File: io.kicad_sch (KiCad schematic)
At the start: 26 parts, among them CN3 DF40C-30DS-0.4V | IO, J1 USB3_A, J6 Micro_SD_Card_Det1, U12 GL850G-HHY22, U7 USBLC6-2P6, Y1 Crystal

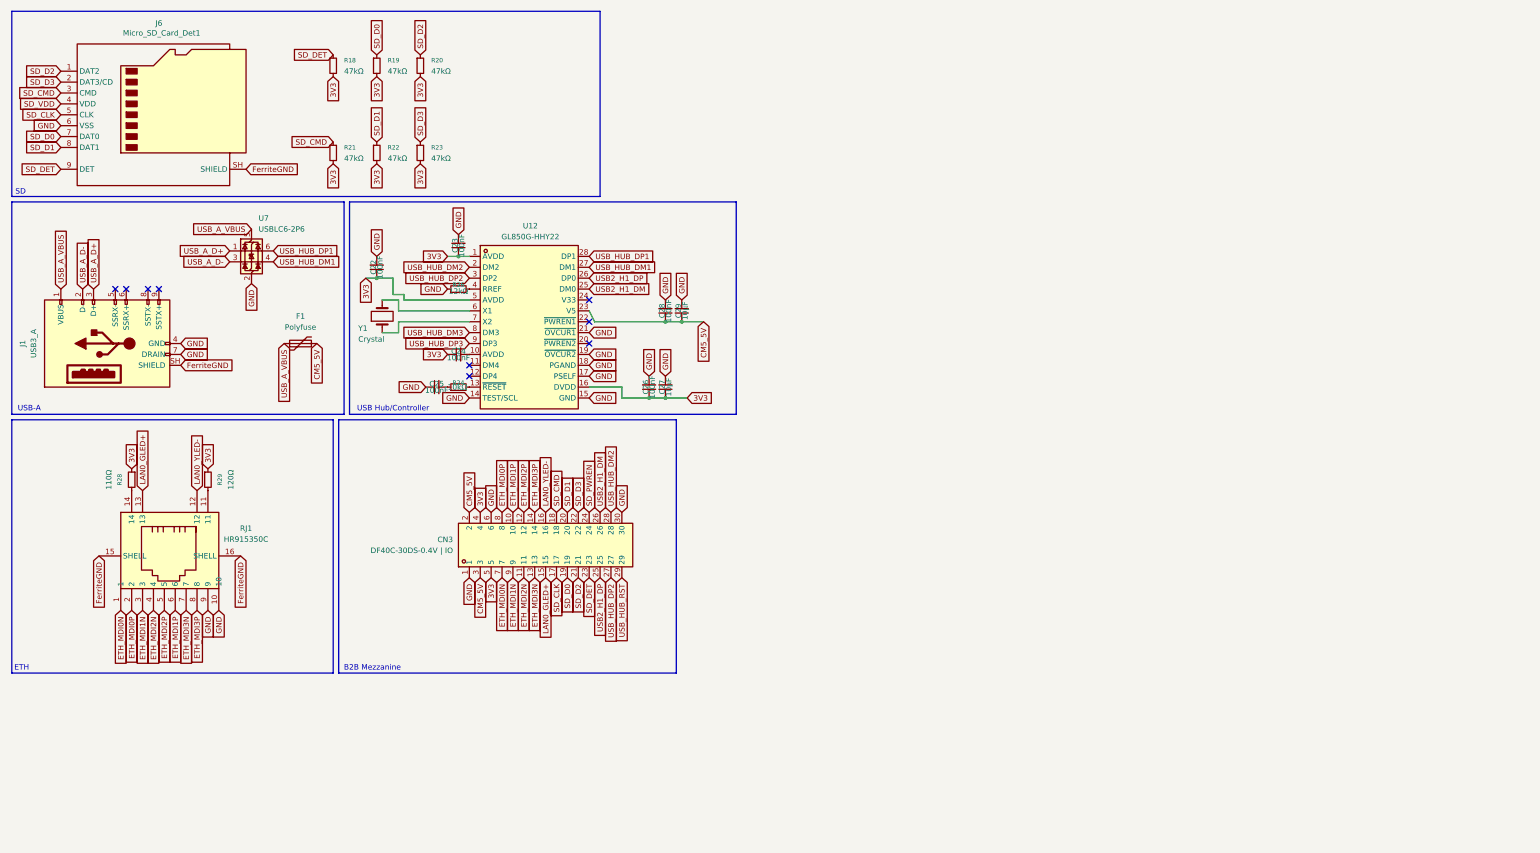
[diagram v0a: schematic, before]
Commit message: Move Data USB-C Port to IO + Add USB1 SS mux and SBU orientation switch, resolve CM5 GPIO assignments
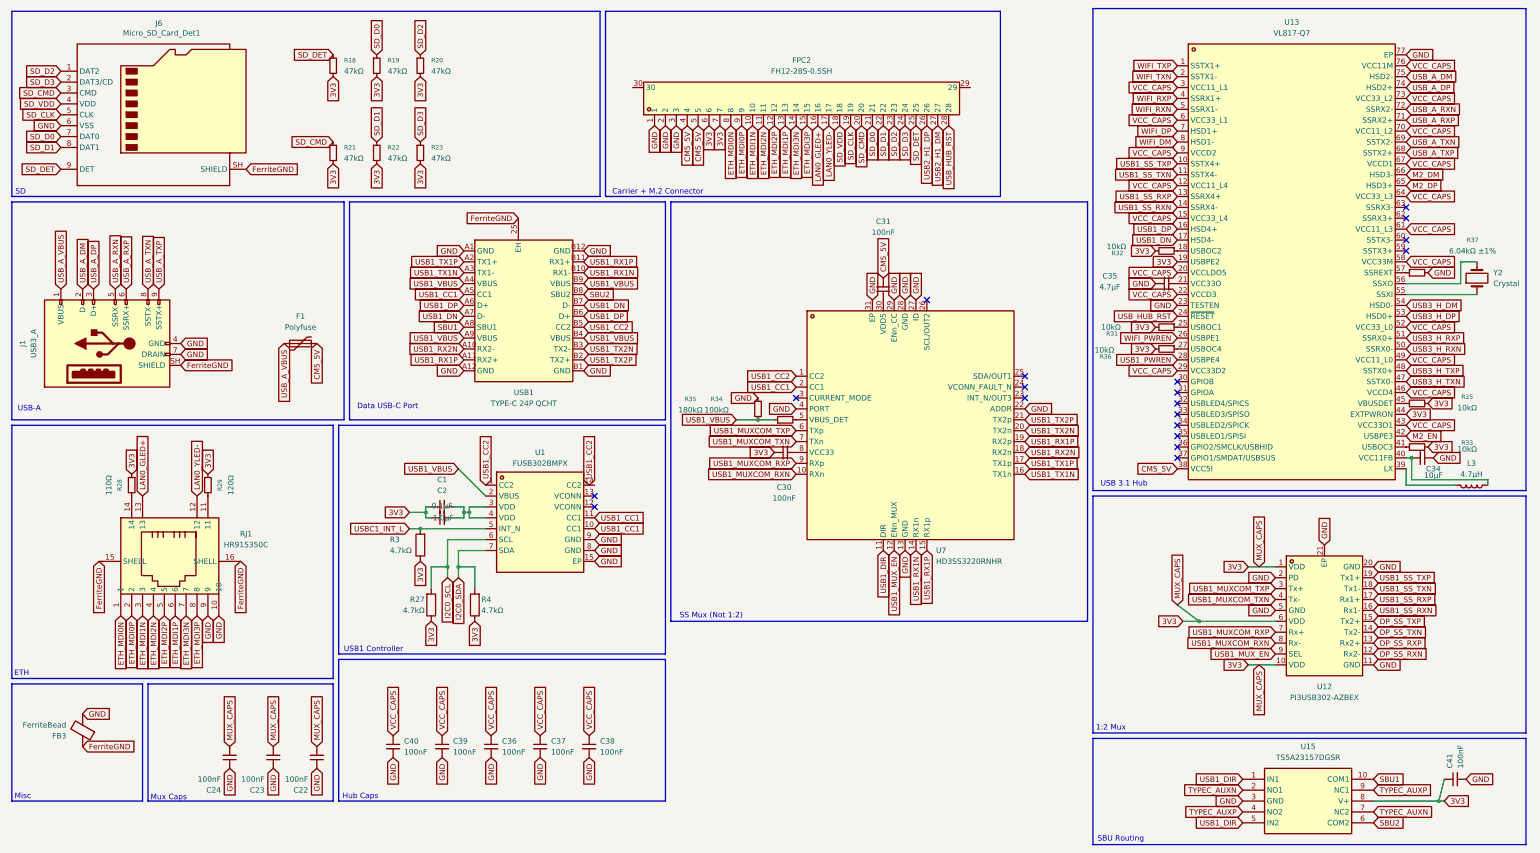
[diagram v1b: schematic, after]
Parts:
- removed C25, C26, C28: 100nF, symbol Device:C_Small
- removed C27, C29: 10µF, symbol Device:C_Small
- removed CN3: DF40C-30DS-0.4V | IO, slate113:CONN-SMD_DF40C-30DS-0.4V51, symbol slate113:DF40C-30DS-0.4V
- removed R24: 10kΩ, symbol Device:R_Small
- removed R26: 12kΩ, symbol Device:R_Small
- removed U12: GL850G-HHY22, slate113:SSOP-28_L10.2-W5.3-P0.65-LS7.8-BL, symbol slate113:GL850G-HHY22
- removed U7: USBLC6-2P6, Package_TO_SOT_SMD:SOT-666, symbol Power_Protection:USBLC6-2P6
- removed Y1: Crystal, symbol Device:Crystal
- added C1: 0.1µF, symbol Device:C_Small
- added C2: 1.0µF, symbol Device:C_Small
- added C30, C31, C36, C37, C38, C39, C40, C41: 100nF, symbol Device:C_Small
- added C34: 10µF, symbol Device:C_Small
- added C35: 4.7µF, symbol Device:C_Small
- added FB3: FerriteBead, symbol Device:FerriteBead
- added FPC2: FH12-28S-0.5SH, slate113:FPC-SMD_28P-P0.50_FH12-28S-0.5SH-55, symbol slate113:FH12-28S-0.5SH
- added L3: 4.7µH, symbol Device:L
- added R25, R31, R32, R33, R36: 10kΩ, symbol Device:R_Small
- added R27, R3, R4: 4.7kΩ, symbol Device:R
- added R34: 100kΩ, symbol Device:R_Small
- added R35: 180kΩ, symbol Device:R_Small
- added R37: 6.04kΩ ±1%, symbol Device:R_Small
- added U1: FUSB302BMPX, slate113:MLP-14_L2.5-W2.5-P0.50-BL-EP, symbol slate113:FUSB302BMPX
- added U12: PI3USB302-AZBEX, slate113:DHVQFN-20_L4.5-W2.5-P0.50-BL-EP, symbol slate113:PI3USB302-AZBEX
- added U13: VL817-Q7, slate113:QFN-76_L9.0-W9.0-P0.40-BL-EP, symbol slate113:VL817-Q7
- added U15: TS5A23157DGSR, slate113:MSOP-10_L3.0-W3.0-P0.50-LS5.0-BL, symbol slate113:TS5A23157DGSR
- added U7: HD3SS3220RNHR, slate113:WQFN-30_L4.5-W2.5-P0.4-BL-EP, symbol slate113:HD3SS3220RNHR
- added USB1: TYPE-C 24P QCHT, slate113:TYPE-C-SMD_TYPE-C-24P-QCHT, symbol slate113:TYPE-C24PQCHT
- added Y2: Crystal, symbol Device:Crystal
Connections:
- net 3V3: now also C22.2, C23.2, C24.2, C1.1, C2.1, C30.1, C41.1, FPC2.6, FPC2.7, R25.2, R27.1, R3.1, R31.2, R32.2, R33.2, R36.2, R4.1, U12.1 (VDD), U12.10 (VDD), U12.6 (VDD), U13.19 (USBPE2), U13.44 (EXTPWRON), U15.8 (V+); no longer C22.1, C23.1, C24.1
- net CM5_5V: now also C31.2, FPC2.4, FPC2.5, U13.38 (VCC5I)
- net ETH_MDI0N: now also FPC2.8
- net ETH_MDI0P: now also FPC2.9
- net ETH_MDI1N: now also FPC2.10
- net ETH_MDI1P: now also FPC2.13
- net ETH_MDI2N: now also FPC2.11
- net ETH_MDI2P: now also FPC2.12
- net ETH_MDI3N: now also FPC2.14
- net ETH_MDI3P: now also FPC2.15
- net FerriteGND: now also FB3.1, USB1.25 (EH)
- net GND: now also C22.1, C23.1, C24.1, C34.1, C35.1, C36.2, C37.2, C38.2, C39.2, C40.2, C41.2, FB3.2, FPC2.1, FPC2.2, FPC2.3, R35.1, R37.2, U1.15 (EP), U1.8 (GND), U1.9 (GND), U12.11 (GND), U12.2 (PD), U12.20 (GND), U12.21 (EP), U12.5 (GND), U13.23 (TESTEN), U13.77 (EP), U15.3 (GND), U7.13 (GND), U7.22 (ADDR), U7.27 (ID), U7.28 (GND), U7.29 (ENn_CC), U7.31 (EP), U7.4 (PORT), USB1.A1 (GND), USB1.A12 (GND), USB1.B1 (GND), USB1.B12 (GND); no longer C22.2, C23.2
- net LAN0_GLED+: now also FPC2.16
- net LAN0_YLED-: now also FPC2.17
- net SD_CLK: now also FPC2.19
- net SD_CMD: now also FPC2.20
- net SD_D0: now also FPC2.21
- net SD_D1: now also FPC2.22
- net SD_D2: now also FPC2.23
- net SD_D3: now also FPC2.24
- net SD_DET: now also FPC2.25
- net SD_VDD: now also FPC2.18
- net USB2_H1_DM: now also FPC2.27
- net USB2_H1_DP: now also FPC2.26
- net USB_HUB_RST: now also FPC2.28, U13.24 (~{RESET})
- net USB_A_RXN: now reaches J1.5 (SSRX-)
- net USB_A_RXN: now also U13.72 (SSRX2-)
- net USB_A_RXP: now reaches J1.6 (SSRX+)
- net USB_A_RXP: now also U13.71 (SSRX2+)
- net USB_A_TXN: now reaches J1.8 (SSTX-)
- net USB_A_TXN: now also U13.69 (SSTX2-)
- net USB_A_TXP: now reaches J1.9 (SSTX+)
- net USB_A_TXP: now also U13.68 (SSTX2+)
- net USB_A_D+ renamed USB_A_DP
- net USB_A_DP: now also U13.74 (HSD2+)
- net USB_A_D- renamed USB_A_DM
- net USB_A_DM: now also U13.75 (HSD2-)
- new net: C31.1, U7.30 (VDD5)
- new net: R31.1, U13.25 (USBOC1)
- new net: C1.2, C2.2, U1.3 (VDD), U1.4 (VDD)
- new net: R32.1, U13.18 (USBOC2)
- new net: C35.2, U13.21 (VCC33O)
- new net: R36.1, U13.27 (USBOC4)
- new net: L3.2, U13.39 (LX)
- new net: C34.2, L3.1, U13.40 (VCC11FB)
- new net: R33.1, U13.41 (USBOC3)
- new net: R25.1, U13.45 (VBUSDET)
- new net: U13.55 (SSXI), Y2.1
- new net: U13.56 (SSXO), Y2.2
- new net: R37.1, U13.57 (SSREXT)
- new net: R34.2, U7.5 (VBUS_DET)
- new net: C30.2, U7.8 (VCC33)
- new net DP_SS_RXN: U12.12 (Rx2-)
- new net DP_SS_RXP: U12.13 (Rx2+)
- new net DP_SS_TXN: U12.14 (Tx2-)
- new net DP_SS_TXP: U12.15 (Tx2+)
- new net I2C0_SCL: R27.2, U1.6 (SCL)
- new net I2C0_SDA: R4.2, U1.7 (SDA)
- new net M2_DM: U13.66 (HSD3-)
- new net M2_DP: U13.65 (HSD3+)
- new net M2_EN: U13.42 (USBPE3)
- new net SBU1: U15.10 (COM1), USB1.A8 (SBU1)
- new net SBU2: U15.6 (COM2), USB1.B8 (SBU2)
- new net TYPEC_AUXN: U15.2 (NO1), U15.7 (NC2)
- new net TYPEC_AUXP: U15.4 (NO2), U15.9 (NC1)
- new net USB1_CC1: U1.10 (CC1), U1.11 (CC1), U7.2 (CC1), USB1.A5 (CC1)
- new net USB1_CC2: U1.1 (CC2), U7.1 (CC2), USB1.B5 (CC2)
- new net USB1_DIR: U15.1 (IN1), U15.5 (IN2), U7.11 (DIR)
- new net USB1_DN: U13.17 (HSD4-), USB1.A7 (D-), USB1.B7 (D-)
- new net USB1_DP: U13.16 (HSD4+), USB1.A6 (D+), USB1.B6 (D+)
- new net USB1_MUXCOM_RXN: U12.8 (Rx-), U7.10 (RXn)
- new net USB1_MUXCOM_RXP: U12.7 (Rx+), U7.9 (RXp)
- new net USB1_MUXCOM_TXN: U12.4 (Tx-), U7.7 (TXn)
- new net USB1_MUXCOM_TXP: U12.3 (Tx+), U7.6 (TXp)
- new net USB1_MUX_EN: U12.9 (SEL), U7.12 (ENn_MUX)
- new net USB1_PWREN: U13.28 (USBPE4)
- new net USB1_RX1N: U7.14 (RX1n), USB1.B10 (RX1-)
- new net USB1_RX1P: U7.15 (RX1p), U7.19 (RX2p), USB1.A11 (RX2+), USB1.B11 (RX1+)
- new net USB1_RX2N: U7.18 (RX2n), USB1.A10 (RX2-)
- new net USB1_SS_RXN: U12.16 (Rx1-), U13.14 (SSRX4-)
- new net USB1_SS_RXP: U12.17 (Rx1+), U13.13 (SSRX4+)
- new net USB1_SS_TXN: U12.18 (Tx1-), U13.11 (SSTX4-)
- new net USB1_SS_TXP: U12.19 (Tx1+), U13.10 (SSTX4+)
- new net USB1_TX1N: U7.16 (TX1n), USB1.A3 (TX1-)
- new net USB1_TX1P: U7.17 (TX1p), USB1.A2 (TX1+)
- new net USB1_TX2N: U7.20 (TX2n), USB1.B3 (TX2-)
- new net USB1_TX2P: U7.21 (TX2p), USB1.B2 (TX2+)
- new net USB1_VBUS: R34.1, R35.2, U1.2 (VBUS), USB1.A4 (VBUS), USB1.A9 (VBUS), USB1.B4 (VBUS), USB1.B9 (VBUS)
- new net USB3_H_DM: U13.54 (HSD0-)
- new net USB3_H_DP: U13.53 (HSD0+)
- new net USB3_H_RXN: U13.50 (SSRX0-)
- new net USB3_H_RXP: U13.51 (SSRX0+)
- new net USB3_H_TXN: U13.47 (SSTX0-)
- new net USB3_H_TXP: U13.48 (SSTX0+)
- new net USBC1_INT_L: R3.2, U1.5 (INT_N)
- new net VCC_CAPS: C36.1, C37.1, C38.1, C39.1, C40.1, U13.12 (VCC11_L4), U13.15 (VCC33_L4), U13.20 (VCCLDO5), U13.22 (VCCD3), U13.29 (VCC33D2), U13.3 (VCC11_L1), U13.43 (VCC33D1), U13.46 (VCCD4), U13.49 (VCC11_L0), U13.52 (VCC33_L0), U13.58 (VCC33M), U13.6 (VCC33_L1), U13.61 (VCC11_L3), U13.64 (VCC33_L3), U13.67 (VCCD1), U13.70 (VCC11_L2), U13.73 (VCC33_L2), U13.76 (VCC11M), U13.9 (VCCD2)
- new net WIFI_DM: U13.8 (HSD1-)
- new net WIFI_DP: U13.7 (HSD1+)
- new net WIFI_PWREN: U13.26 (USBPE1)
- new net WIFI_RXN: U13.5 (SSRX1-)
- new net WIFI_RXP: U13.4 (SSRX1+)
- new net WIFI_TXN: U13.2 (SSTX1-)
- new net WIFI_TXP: U13.1 (SSTX1+)
- no-connect marks 9 -> 19
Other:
- note added: "1:2 Mux"
- note added: "Carrier + M.2 Connector"
- note added: "Data USB-C Port"
- note added: "Hub Caps"
- note added: "Misc"
- note added: "Mux Caps"
- note added: "SBU Routing"
- note added: "SS Mux (Not 1:2)"
- note added: "USB 3.1 Hub"
- note added: "USB1 Controller"
- note removed: "B2B Mezzanine"
- note removed: "USB Hub/Controller"
- moved on the sheet: R28, R29, RJ1

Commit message: add wifi+ble combo symbol, fix connector pin counts, slim b2b connectors, drop 3-way flex cable
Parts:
- removed C35: 4.7µF, symbol Device:C_Small
- removed FPC2: FH12-28S-0.5SH, slate113:FPC-SMD_28P-P0.50_FH12-28S-0.5SH-55, symbol slate113:FH12-28S-0.5SH
- added C18, C32, C42: 2.2µF, symbol Device:C_Small
- added C20, C26, C27, C33, C43, C44, C45, C46, C47, C48, C49, C50, C51, C52, C53, C54, C55, C56: 100nF, symbol Device:C_Small
- added CN2: DF40C-40DP-0.4V, slate113:CONN-SMD_DF40C-40DP-0.4V, symbol slate113:DF40C-40DP-0.4V
- added R24: 10kΩ, symbol Device:R_Small
- added U10, U14, U17: SiP32508DT, Package_TO_SOT_SMD:TSOT-23-6, symbol Power_Management:SiP32508DT
- added U16: (no value), symbol slate113:AMLGA7921
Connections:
- net 3V3: now also C18.1, C42.1, CN2.6, CN2.7, R24.1
- net CM5_5V: now also C32.1, CN2.4, CN2.5
- net DP_SS_RXN: now also CN2.34
- net DP_SS_RXP: now also CN2.33
- net DP_SS_TXN: now also CN2.32
- net DP_SS_TXP: now also CN2.31
- net ETH_MDI0N: now also CN2.8
- net ETH_MDI0P: now also CN2.9
- net ETH_MDI1N: now also CN2.10
- net ETH_MDI1P: now also CN2.13
- net ETH_MDI2N: now also CN2.11
- net ETH_MDI2P: now also CN2.12
- net ETH_MDI3N: now also CN2.14
- net ETH_MDI3P: now also CN2.15
- net FerriteGND: now also CN2.39, CN2.41, CN2.42, CN2.43, CN2.44
- net GND: now also C26.1, C27.1, C44.2, C45.2, C46.2, C47.2, C48.2, C49.2, C50.2, C51.2, C52.2, C53.2, C54.2, C55.2, C56.2, CN2.1, CN2.2, CN2.3, U10.4 (GND), U14.4 (GND), U16.14 (GND), U16.15 (GND), U16.18 (GND), U16.19 (GND), U16.21 (GND), U16.22 (GND), U16.29 (GND), U16.3 (GND), U16.6 (GND), U16.9 (GND), U17.4 (GND)
- net I2C0_SCL: now also CN2.37
- net I2C0_SDA: now also CN2.38
- net LAN0_GLED+: now also CN2.16
- net LAN0_YLED-: now also CN2.17
- net M2_DM: now also CN2.27
- net M2_DP: now also CN2.26
- net M2_EN: now also CN2.40
- net SD_CLK: now also CN2.19
- net SD_CMD: now also CN2.20
- net SD_D0: now also CN2.21
- net SD_D1: now also CN2.22
- net SD_D2: now also CN2.23
- net SD_D3: now also CN2.24
- net SD_DET: now also CN2.25
- net SD_VDD: now also C20.1
- net TYPEC_AUXN: now also CN2.36
- net TYPEC_AUXP: now also CN2.35
- net USB1_DIR: now also CN2.30
- net USB1_MUX_EN: now also CN2.29
- net USB1_PWREN: now also U14.3 (EN)
- net USB1_VBUS: now also C33.1
- net USB_HUB_RST: now also CN2.28
- net VCC_CAPS: now also U13.21 (VCC33O), C44.1, C45.1, C46.1, C47.1, C48.1, C49.1, C50.1, C51.1, C52.1, C53.1, C54.1, C55.1, C56.1
- net WIFI_DM: now also U16.8 (USB_DM)
- net WIFI_DP: now also U16.7 (USB_DP)
- net WIFI_PWREN: now also U17.3 (EN)
- net WIFI_RXN: now also U16.4 (SSUSB_RXN)
- net WIFI_RXP: now also U16.5 (SSUSB_RXP)
- net WIFI_TXN: now also U16.1 (SSUSB_TXN)
- net WIFI_TXP: now also U16.2 (SSUSB_TXP)
- new net: C32.2, U14.5 (IN), U14.6 (IN)
- new net: C43.2, U17.1 (OUT), U17.2 (OUT)
- new net: C20.2, U10.1 (OUT), U10.2 (OUT)
- new net: C18.2, U10.5 (IN), U10.6 (IN)
- new net: R24.2, U16.26 (#RST)
- new net: C42.2, U17.5 (IN), U17.6 (IN)
- new net: C33.2, U14.1 (OUT), U14.2 (OUT)
- new net BT_WAKE: U16.11 (#BT_WAKE)
- new net SD_PWREN: CN2.18, U10.3 (EN)
- new net WIFI_CAPS: C26.2, C27.2, C43.1, U16.27 (DVDD), U16.28 (DVDD)
- new net WOWLAN: U16.10 (#WOWLAN)
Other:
- note added: "Controller"
- note added: "SD Power"
- note added: "USB1 Power"
- note added: "WiFi Module"
- note added: "WiFi Power"
- moved on the sheet: C36, C37, C38, C39, C40

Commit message: finish wiring up usb hub + fix stale nets + address DRC errors
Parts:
- removed CN2: DF40C-40DP-0.4V, slate113:CONN-SMD_DF40C-40DP-0.4V, symbol slate113:DF40C-40DP-0.4V
- added CN1: DF40C-50DP-0.4V, slate113:CONN-SMD_DF40C-50DP-0.4V, symbol slate113:DF40C-50DP-0.4V
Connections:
- net 3V3: now also CN1.6, CN1.7
- net CM5_5V: now also CN1.4, CN1.5
- net DP_SS_RXN: now also CN1.34
- net DP_SS_RXP: now also CN1.33
- net DP_SS_TXN: now also CN1.32
- net DP_SS_TXP: now also CN1.31
- net ETH_MDI0N: now also CN1.8
- net ETH_MDI0P: now also CN1.9
- net ETH_MDI1N: now also CN1.10
- net ETH_MDI1P: now also CN1.13
- net ETH_MDI2N: now also CN1.11
- net ETH_MDI2P: now also CN1.12
- net ETH_MDI3N: now also CN1.14
- net ETH_MDI3P: now also CN1.15
- net FerriteGND: no longer FB3.1
- net GND: now also CN1.1, CN1.2, CN1.3, CN1.39, CN1.43, CN1.44
- net I2C0_SCL: now also CN1.37
- net I2C0_SDA: now also CN1.38
- net LAN0_GLED+: now also CN1.16
- net LAN0_YLED-: now also CN1.17
- net M2_DM: now also CN1.27
- net M2_DP: now also CN1.26
- net M2_EN: now also CN1.40
- net SD_CLK: now also CN1.19
- net SD_CMD: now also CN1.20
- net SD_D0: now also CN1.21
- net SD_D1: now also CN1.22
- net SD_D2: now also CN1.23
- net SD_D3: now also CN1.24
- net SD_DET: now also CN1.25
- net SD_PWREN: now also CN1.18
- net TYPEC_AUXN: now also CN1.36
- net TYPEC_AUXP: now also CN1.35
- net USB1_DIR: now also CN1.30
- net USB1_MUX_EN: now also CN1.29
- net USB_HUB_RST: now also CN1.28
- net USB3_H_DM renamed USB2_H_DM
- net USB2_H_DM: now also CN1.42
- net USB3_H_DP renamed USB2_H_DP
- net USB2_H_DP: now also CN1.41
- new net FerriteGND_IO: CN1.51, CN1.52, CN1.53, CN1.54, FB3.1
- no-connect marks 19 -> 29
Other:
- note added: "PWR Declarations"
- moved on the sheet: FB3

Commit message: forgot to save
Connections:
- net USB1_CC2: now also U1.14 (CC2)

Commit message: finished gps schematic, updated footprints and 3d models
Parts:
- J1: footprint (none) -> slate113:HC-USB3_0-L168-WJ_COPY
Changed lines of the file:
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@@
 			)
 		)
-		(property "Footprint" ""
+		(property "Footprint" "slate113:HC-USB3_0-L168-WJ_COPY"
 			(at 33.02 87.63 0)
 			(hide yes)

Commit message: finished radio board with load switches and flash, fixed b2b connector, started antenna module and rf sense switching circuit
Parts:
- added C93: 8.2pF, symbol Device:C_Small
- added C94: 0.1µF, symbol Device:C_Small
- added C99: 100pF, symbol Device:C_Small
- added J13: WiFi SMA, symbol Connector:Conn_Coaxial_Small
- added J14: BLE SMA, symbol Connector:Conn_Coaxial_Small
- added J15: WiFi PATCH, symbol Connector:Conn_Coaxial_Small
- added J16, J17: BLE PATCH, symbol Connector:Conn_Coaxial_Small
- added J18: WIFI PATCH, symbol Connector:Conn_Coaxial_Small
- added R45, R46: 50Ω, symbol Device:R_Small
- added R47: 10kΩ, symbol Device:R_Small
- added U30, U36: PE4259-63, slate113:SC-70-6_L2.2-W1.3-P0.65-LS2.1-BL, symbol slate113:PE4259-63
- added U37: 2450CF15A0100001E, symbol slate113:2450CF15A0100001E
- added U38: X4C60K1-20S, symbol slate113:X4C60K1-20S
- added U39: XEC24P3-30G, symbol slate113:X4C60K1-20S
- added U40, U41, U42: AD8317ACPZ-R7, slate113:LFCSP-8_L3.0-W2.0-P0.50-BL-EP, symbol slate113:AD8317ACPZ-R7
- added U43: LM339D, slate113:SOIC-14_L8.7-W3.9-P1.27-LS6.0-BL, symbol slate113:LM339D
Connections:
- net GND: now also C93.2, C94.2, C99.2, J13.2 (Ext), J14.2 (Ext), J15.2 (Ext), J16.2 (Ext), J17.2 (Ext), J18.2 (Ext), R45.2, R46.2, R47.2, U30.2 (GND), U36.2 (GND), U37.2 (GND), U37.3 (GND), U37.6 (GND), U37.7 (GND), U40.2 (COMM), U40.9 (EP)
- net WIFI_CTRL: now reaches CN1.45
- net WIFI_CTRL: now also U30.4 (CTRL)
- net BLE_CTRL: now reaches CN1.46
- net BLE_CTRL: now also U36.4 (CTRL)
- net WIFI_ANT0: now reaches U16.33 (WIFI0)
- net WIFI_ANT0: now also J18.1 (In)
- net WIFI_ANT1: now reaches U16.34 (WIFI1)
- net WIFI_ANT1: now also U30.5 (RFC)
- net BLE_ANT0: now reaches U16.35 (BT0)
- net BLE_ANT0: now also J17.1 (In)
- net BLE_ANT1: now reaches U16.36 (BT1)
- net BLE_ANT1: now also U36.5 (RFC)
- net 3V3 renamed 24G_VPOS_CAPS
- net 24G_VPOS_CAPS: now also U30.6 (CTRL#orVDD), U36.6 (CTRL#orVDD), U40.7 (VPOS)
- new net: J16.1 (In), U36.1 (RF1)
- new net: C93.1, U40.3 (CLPF)
- new net: J15.1 (In), U30.1 (RF1)
- new net: R47.1, U40.6 (TADJ)
- new net BLE_CPL: U37.5 (Coupled_Out)
- new net BLE_SMA_ANT: J14.1 (In), U37.8 (Output)
- new net BLE_SW_SMA: U36.3 (RF2), U37.4 (Input)
- new net VPOS_CAPS: C94.1, C99.1
- new net WIFI_2.4G_5G: U38.1 (Input), U39.2 (Direct)
- new net WIFI_2.4G_CPL: U39.4 (Coupled)
- new net WIFI_2.4G_ISO: R46.1, U39.3 (Isolated)
- new net WIFI_24G_CPL: U40.1 (INHI)
- new net WIFI_24G_DET: U40.4 (VSET), U40.5 (VOUT)
- new net WIFI_5G_CPL: U38.4 (Coupled)
- new net WIFI_5G_ISO: R45.1, U38.3 (Isolated)
- new net WIFI_SMA_ANT: J13.1 (In), U38.2 (Direct)
- new net WIFI_SW_SMA: U30.3 (RF2), U39.1 (Input)
- no-connect marks 29 -> 25
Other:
- note added: "ANT Throws"
- note added: "Caps"
- note added: "RF-Sense"
- note removed: "Hub Caps"
- moved on the sheet: C26, C27, C55, C56

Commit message: finished rf sense and io board closure, added audio system with pcm and three spdt switches, made changes tp lte module, added ldo and sd/sim slot, updated m.2/audio schematics, added new mic msop qfn sot footprints, and added a protection system for non EM06-A Cards
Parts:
- removed C18: 2.2µF, symbol Device:C_Small
- removed C20: 100nF, symbol Device:C_Small
- removed J6: Micro_SD_Card_Det1, symbol Connector:Micro_SD_Card_Det1
- removed R18, R19, R20, R21, R22, R23: 47kΩ, symbol Device:R_Small
- removed U10: SiP32508DT, Package_TO_SOT_SMD:TSOT-23-6, symbol Power_Management:SiP32508DT
- added C100, C101, C104, C105, C107: 100pF, symbol Device:C_Small
- added C102, C103: 8.2pF, symbol Device:C_Small
- added C106, C108: 0.1µF, symbol Device:C_Small
- added R48, R49, R51: 52.3Ω, symbol Device:R_Small
- added R50, R52, R53, R54, R55: 10kΩ, symbol Device:R_Small
- added R56, R58, R60: 100kΩ, symbol Device:R_Small
- added R57, R59, R61: 20kΩ, symbol Device:R_Small
- U16: value (none) -> AMLGA7921
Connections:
- net 24G_VPOS_CAPS is gone; now on net 2.4G_SENSE: C1.1, C2.1, C22.2, C23.2, C24.2, C30.1, C41.1, C42.1, CN1.6, CN1.7, R24.1, R25.2, R27.1, R28.1, R29.1, R3.1, R31.2, R32.2, R33.2, R36.2, R4.1, U12.1 (VDD), U12.10 (VDD), U12.6 (VDD), U13.19 (USBPE2), U13.44 (EXTPWRON), U15.8 (V+), U30.6 (CTRL#orVDD), U36.6 (CTRL#orVDD), U40.7 (VPOS)
- net VPOS_CAPS is gone; now on net 2.4G_SENSE: C94.1, C99.1
- net WIFI_24G_DET is gone; now on net WIFI_2.4G_DET: U40.4 (VSET), U40.5 (VOUT)
- net BLE_CPL: now also R51.2
- net GND: now also CN1.50, U41.2 (COMM), U41.9 (EP), U42.2 (COMM), U42.9 (EP), U43.11, U43.12 (GND), C102.2, C103.2, C105.2, C106.2, C107.2, C108.2, R50.2, R52.2, R57.2, R59.2, R61.2
- net SD_CLK: no longer CN1.19
- net SD_PWREN: no longer CN1.18
- net WIFI_2.4G_CPL: now also R49.2
- net WIFI_5G_CPL: now also R48.2
- net 2.4G_SENSE: now reaches CN1.47
- net 2.4G_SENSE: now also CN1.48, CN1.49, U41.7 (VPOS), U42.7 (VPOS), U43.10, U43.3 (VDD), C105.1, C106.1, C107.1, C108.1, R53.1, R54.1, R55.1, R56.1, R58.1, R60.1
- net at U43.1: now also R54.2
- net at U43.14: now also R55.2
- net at U43.2: now also R53.2
- net WIFI_2.4G_REF: now reaches U43.4
- net WIFI_2.4G_REF: now also R56.2, R57.1
- net WIFI_2.4G_DET: now reaches U43.5
- net WIFI_5G_REF: now reaches U43.6
- net WIFI_5G_REF: now also R58.2, R59.1
- net WIFI_5G_DET: now reaches U43.7
- net WIFI_5G_DET: now also U41.4 (VSET), U41.5 (VOUT)
- net BLE_DET: now reaches U43.8
- net BLE_DET: now also U42.4 (VSET), U42.5 (VOUT)
- net BLE_REF: now reaches U43.9
- net BLE_REF: now also R60.2, R61.1
- net at U42.1 (INHI): now also C104.2
- net at U42.3 (CLPF): now also C103.1
- net at U42.6 (TADJ): now also R52.1
- net at U41.1 (INHI): now also C100.2
- net at U41.3 (CLPF): now also C102.1
- net at U41.6 (TADJ): now also R50.1
- net SD_CMD: no longer names the net of CN1.20
- net SD_D0: no longer names the net of CN1.21
- net SD_D1: no longer names the net of CN1.22
- net SD_D2: no longer names the net of CN1.23
- net SD_D3: no longer names the net of CN1.24
- net SD_DET: no longer names the net of CN1.25
- net WIFI_24G_CPL: no longer names the net of U40.1 (INHI)
- net WIFI_24G_CPL: now also C101.2
- new net: C104.1, R51.1
- new net: C101.1, R49.1
- new net: C100.1, R48.1
- no-connect marks 25 -> 32
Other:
- note added: "Dividers"
- note removed: "SD"
- note removed: "SD Power"
- moved on the sheet: C55, C56, C94, C99, R28, R29, RJ1, U42, U43
